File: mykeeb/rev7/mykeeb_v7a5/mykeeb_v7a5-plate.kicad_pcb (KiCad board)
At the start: 2 copper layers, 175.6 x 131 mm, 28 parts

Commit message: add gerbers
Signed-off-by: Maximilian Huber <gh@maxhbr.de>
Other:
- board size 175.6 x 131 mm -> 165.5 x 125.7 mm
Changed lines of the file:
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@@
       (drillshape 0)
       (scaleselection 1)
-      (outputdirectory "gerber")
+      (outputdirectory "gerber-plate")
     )
   )
@@
   (gr_arc locked (start 17.85939 58.340674) (mid 18.905567 55.814973) (end 21.431268 54.768796)
     (stroke (width 0.1) (type default)) (layer "Edge.Cuts"))
-  (gr_rect (start 179.189213 37.504719) (end 186.928282 43.457849)
-    (stroke (width 0.0381) (type default)) (fill none) (layer "Edge.Cuts"))
   (gr_line locked (start 49.410979 56.554735) (end 49.410979 44.648475)
     (stroke (width 0.0381) (type default)) (layer "Edge.Cuts"))
@@
   (gr_circle locked (center 38.695345 98.226645) (end 39.885971 98.226645)
     (stroke (width 0.0381) (type default)) (fill none) (layer "Edge.Cuts"))
-  (gr_rect (start 179.784526 38.100032) (end 186.332969 42.862536)
-    (stroke (width 0.0381) (type default)) (fill none) (layer "Edge.Cuts"))
-  (gr_rect (start 181.570465 39.885971) (end 184.54703 41.076597)
-    (stroke (width 0.0381) (type default)) (fill none) (layer "Edge.Cuts"))
   (gr_circle locked (center 98.821958 113.10947) (end 100.012584 113.10947)
     (stroke (width 0.0381) (type default)) (fill none) (layer "Edge.Cuts"))
@@
   (gr_line locked (start 35.123467 44.648475) (end 35.123467 56.554735)
     (stroke (width 0.0381) (type default)) (layer "Edge.Cuts"))
-  (gr_rect (start 11.310947 162.520449) (end 19.050016 168.473579)
-    (stroke (width 0.0381) (type default)) (fill none) (layer "Edge.Cuts"))
   (gr_line locked (start 75.487943 124.420403) (end 60.721926 124.420417)
     (stroke (width 0.1) (type default)) (layer "Edge.Cuts"))
   (gr_line locked (start 105.965714 49.410979) (end 113.10947 49.410979)
     (stroke (width 0.1) (type default)) (layer "Edge.Cuts"))
-  (gr_rect (start 13.096886 164.306388) (end 17.264077 166.68764)
-    (stroke (width 0.0381) (type default)) (fill none) (layer "Edge.Cuts"))
   (gr_arc locked (start 49.410979 44.648475) (mid 50.457158 42.122775) (end 52.982857 41.076597)
     (stroke (width 0.1) (type default)) (layer "Edge.Cuts"))
@@
   (gr_circle locked (center 137.517303 97.036019) (end 138.707929 97.036019)
     (stroke (width 0.0381) (type default)) (fill none) (layer "Edge.Cuts"))
-  (gr_rect (start 180.975152 39.290658) (end 185.142343 41.67191)
-    (stroke (width 0.0381) (type default)) (fill none) (layer "Edge.Cuts"))
   (gr_curve locked (pts (xy 135.731364 132.754799) (xy 143.470433 137.517303) (xy 144.706509 138.970727) (xy 149.469013 143.733231))
     (stroke (width 0.16) (type solid)) (layer "Edge.Cuts"))
@@
   (gr_arc locked (start 26.789085 51.196918) (mid 25.742908 53.722619) (end 23.217207 54.768796)
     (stroke (width 0.1) (type default)) (layer "Edge.Cuts"))
-  (gr_rect (start 11.90626 163.115762) (end 18.454703 167.878266)
-    (stroke (width 0.0381) (type default)) (fill none) (layer "Edge.Cuts"))
-  (gr_rect (start 13.692199 164.901701) (end 16.668764 166.092327)
-    (stroke (width 0.0381) (type default)) (fill none) (layer "Edge.Cuts"))
   (gr_line locked (start 152.995441 87.511011) (end 152.995441 54.173483)
     (stroke (width 0.1) (type default)) (layer "Edge.Cuts"))

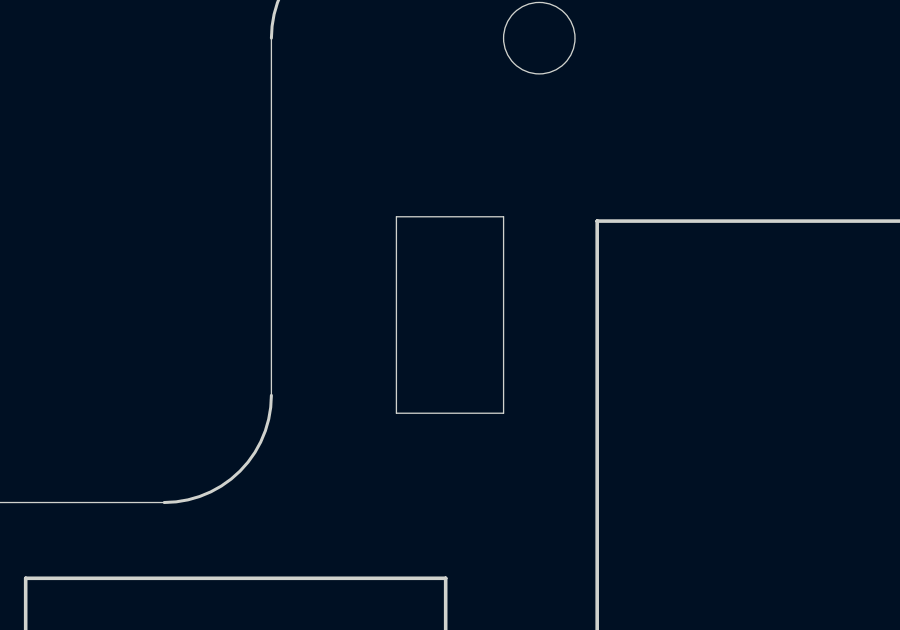
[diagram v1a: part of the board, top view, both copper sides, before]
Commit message: fix the small 'MCU on the wrong side' issue
Signed-off-by: Maximilian Huber <gh@maxhbr.de>
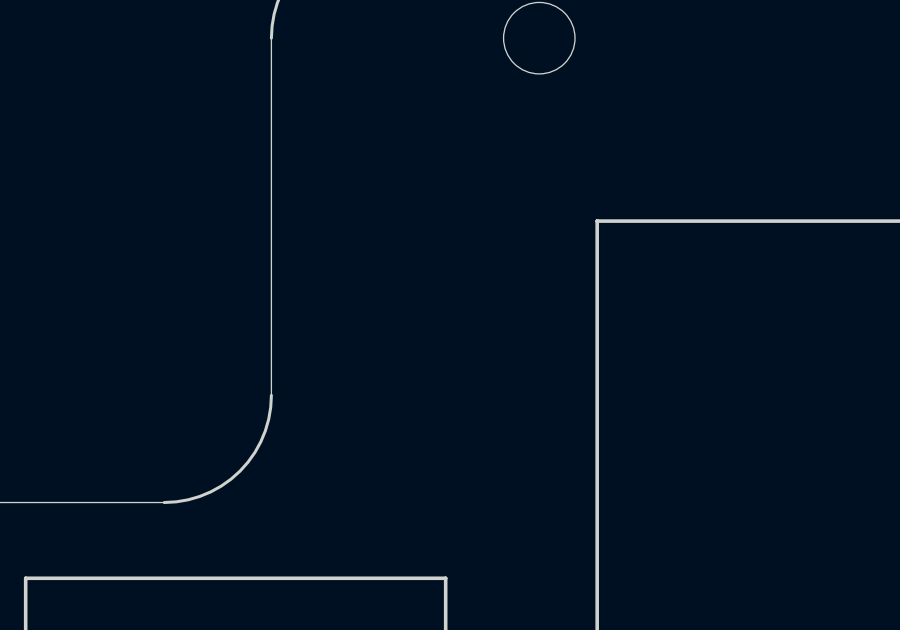
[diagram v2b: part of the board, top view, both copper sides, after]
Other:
- outline, holes or cut-outs redrawn
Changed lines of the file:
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@@
   (gr_circle locked (center 38.695345 79.176629) (end 39.885971 79.176629)
-    (stroke (width 0.0381) (type default)) (fill none) (layer "Edge.Cuts"))
-  (gr_rect locked (start 53.57817 50.601605) (end 57.150048 57.150048)
     (stroke (width 0.0381) (type default)) (fill none) (layer "Edge.Cuts"))
   (gr_circle locked (center 154.78138 122.634478) (end 155.972006 122.634478)
